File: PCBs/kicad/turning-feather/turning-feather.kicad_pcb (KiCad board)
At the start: 2 copper layers, 64.8 x 52.6 mm, 21 parts, among them J1 Out to RJ45, J2 Buttons/beep, J3 Off switch, U1 TSR 1-2450, U2 MIC4427, U3 MIC4427, U4 ZPT

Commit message: Add serial output from ZPT to serial in on feather. PCB V0.23.
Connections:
- U4 pad 6: Net-(U4-Pad6) -> Net-(JP1-Pad14)
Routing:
- net Net-(JP1-Pad14): track 0.00 -> 12.3 mm
- net +12V: track 43.0 -> 51.2 mm
- net Net-(D1-Pad2): track 4.27 -> 8.55 mm
- net Net-(JP1-Pad23): track 40.9 -> 44.3 mm
- net Net-(J2-Pad3): track 41.3 -> 43.0 mm
- net (no net): track 0.76 -> 0.00 mm
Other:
- board text added: "V0.23"
- board text removed: "V0.21"

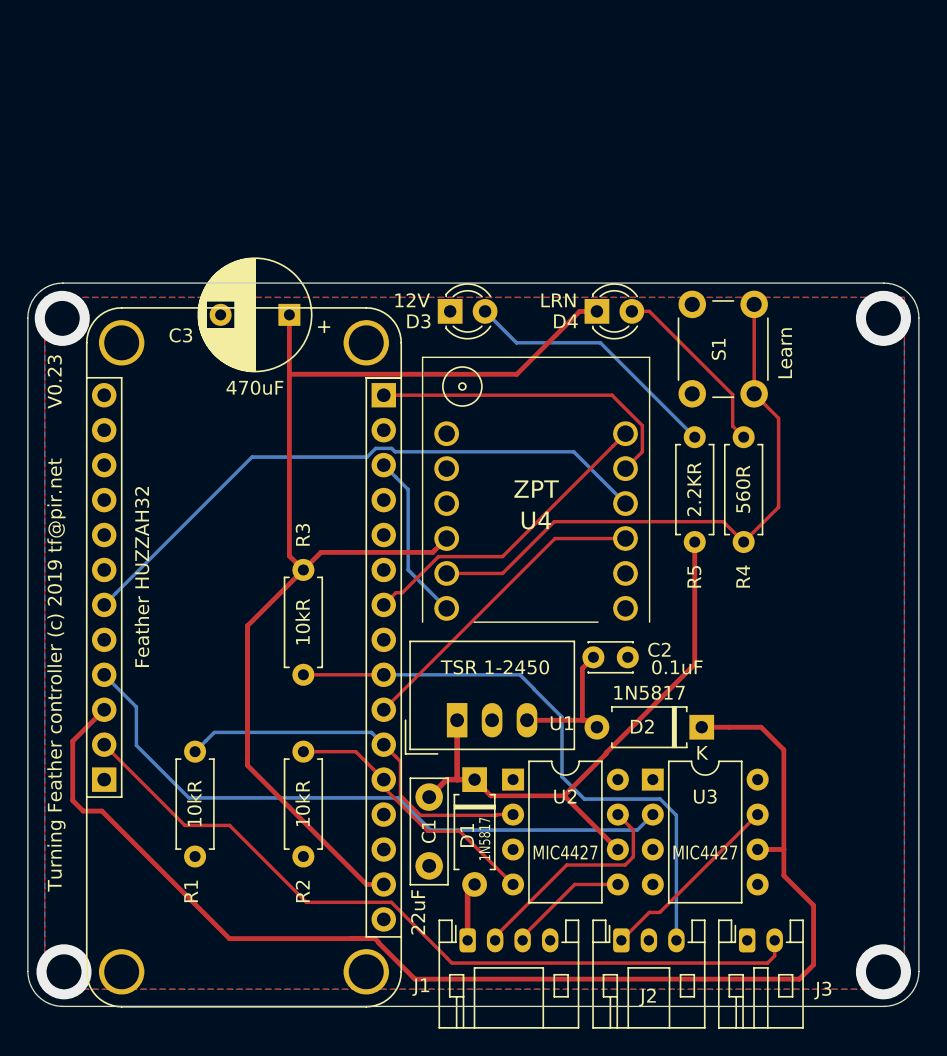
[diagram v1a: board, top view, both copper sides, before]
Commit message: PCB version 0.32.
Add serial connection from ZPT to Serial2 on HUZZAH32.
Connect spare 5V MOSFET input to spare HUZZAH32 output with header.
Add on-board PCB mount RJ45 as an option, old connector retained.
Move LEDs out to new board extension back to point towards user.
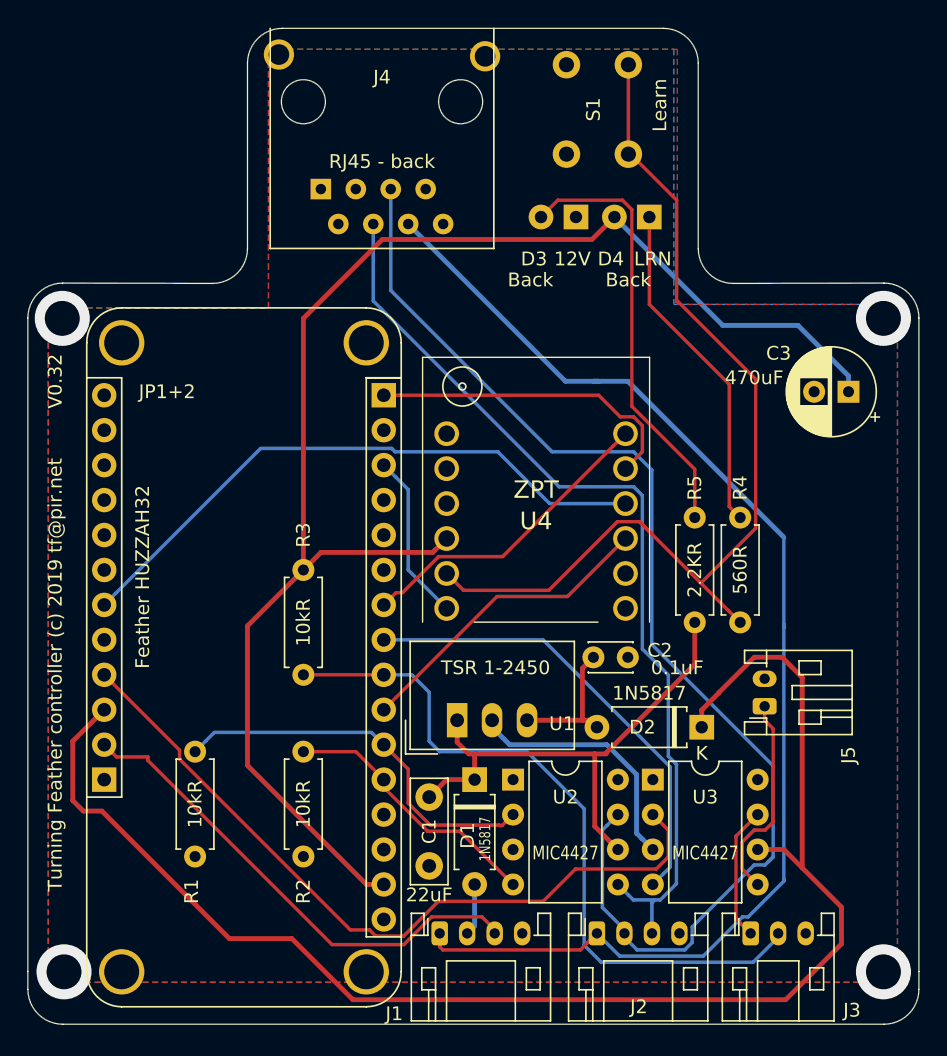
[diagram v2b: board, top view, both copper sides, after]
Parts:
- removed the J2 at (147.8, 160.8)
- added J1: Out to power switch, Connector_JST:JST_PH_S4B-PH-K_1x04_P2.00mm_Horizontal, F.Cu at (134.6, 160.3)
- added J4: RJ45_Shielded, turning-feather:RJ45_Horizontal_Shielded, B.Cu at (126.0, 106.2)
- added J5: Currently unused, Connector_JST:JST_PH_S2B-PH-K_1x02_P2.00mm_Horizontal, F.Cu at (158.2, 143.8)
- C3: footprint Capacitor_THT:CP_Radial_D8.0mm_P5.00mm -> Capacitor_THT:CP_Radial_D6.3mm_P2.50mm
- D3, D4, S1: moved to B.Cu
- J3: value Off switch -> Buttons/beep; footprint Connector_JST:JST_PH_S2B-PH-K_1x02_P2.00mm_Horizontal -> Connector_JST:JST_PH_S3B-PH-K_1x03_P2.00mm_Horizontal
- moved C3 41.0 mm to (164.3, 120.9)
- moved S1 14.2 mm to (148.3, 103.6), turned to 90 degrees
- moved D3 11.4 mm to (144.5, 108.2), turned to 180 degrees
- moved J2 9.41 mm to (146.1, 160.3)
- moved D4 7.85 mm to (149.9, 108.2), turned to 180 degrees
- moved R4 5.85 mm to (156.5, 137.7)
- moved R5 5.84 mm to (153.2, 137.7)
- moved J3 0.57 mm to (157.2, 160.3)
- renumbered J1 to J2, JP1 to JP1+2
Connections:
- D4 pad 1: +3V3 -> Net-(D4-Pad1)
- D4 pad 2: Net-(D4-Pad2) -> +3V3
- J2 pad 1: Net-(D1-Pad2) -> Net-(J1-Pad1)
- J3 pad 1: GND -> Net-(J3-Pad1)
- JP1+2 pad 27: Net-(J3-Pad2) -> Net-(J1-Pad3)
- JP1+2 pad 8: Net-(J2-Pad3) (its old number) -> Net-(J3-Pad2)
- JP1+2 pad 9: Net-(JP1-Pad9) -> Net-(JP1+2-Pad9)
- R3 pad 2: Net-(J2-Pad3) (its old number) -> Net-(J3-Pad2)
- R4 pad 2: Net-(D4-Pad2) -> Net-(D4-Pad1)
- U3 pad 4: Net-(U3-Pad4) -> Net-(JP1+2-Pad9)
- U3 pad 7: Net-(J2-Pad1) -> Net-(J3-Pad1)
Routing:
- net Net-(J1-Pad1): track 0.00 -> 91.9 mm
- net Net-(J2-Pad2): track 16.3 -> 88.7 mm
- net Net-(J2-Pad3): track 8.77 -> 68.0 mm
- net Net-(J2-Pad3) (its old number): track 43.0 -> 0.00 mm
- net Net-(J1-Pad3): track 0.00 -> 36.0 mm
- net Net-(JP1+2-Pad9): track 0.00 -> 33.7 mm
- net Net-(R4-Pad1): track 42.8 -> 71.2 mm
- net Net-(D4-Pad1): track 0.00 -> 24.6 mm
- net +3V3: track 84.0 -> 107.6 mm
- net GND: track 0.00 -> 18.9 mm
- net Net-(J5-Pad1): track 0.00 -> 15.1 mm
- net Net-(J2-Pad1): track 13.7 -> 0.00 mm
- net Net-(D4-Pad2): track 13.3 -> 0.00 mm
- net +12V: track 51.2 -> 38.4 mm
- net Net-(D3-Pad2): track 19.0 -> 31.7 mm
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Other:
- board size 64.8 x 52.6 mm -> 64.8 x 72.4 mm
- board text added: "12V in"
- board text added: "12V out"
- board text added: "Back"
- board text added: "V0.32"
- board text removed: "V0.23"

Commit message: Move ethernet on-PCB, move most things around, change capacitors, etc
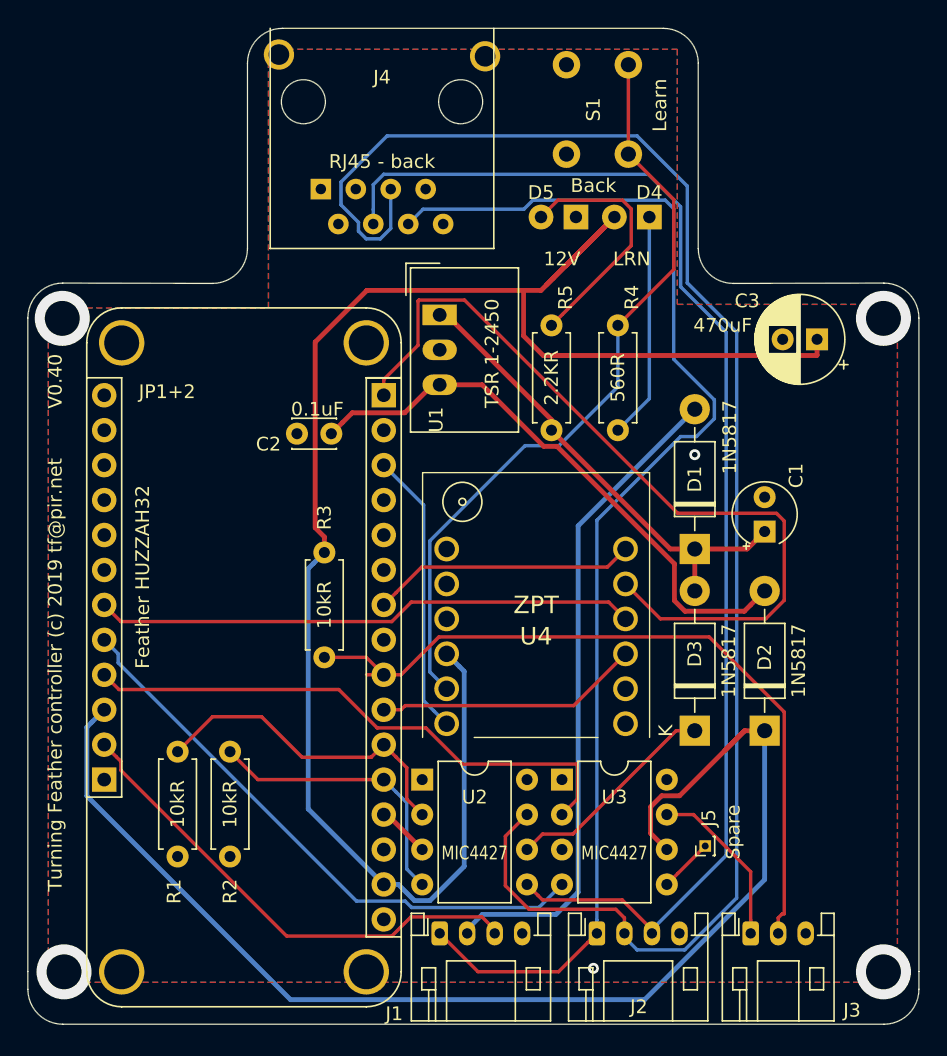
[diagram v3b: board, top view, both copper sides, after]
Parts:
- added D3: 1N5817, Diode_THT:D_DO-41_SOD81_P10.16mm_Horizontal, F.Cu at (153.2, 145.5)
- C1: footprint Capacitor_THT:C_Disc_D7.5mm_W2.5mm_P5.00mm -> Capacitor_THT:CP_Radial_Tantal_D4.5mm_P2.50mm
- D1, D2: footprint Diode_THT:D_A-405_P7.62mm_Horizontal -> Diode_THT:D_DO-41_SOD81_P10.16mm_Horizontal
- J5: value Currently unused -> Spare; footprint Connector_JST:JST_PH_S2B-PH-K_1x02_P2.00mm_Horizontal -> Connector_PinHeader_1.00mm:PinHeader_1x01_P1.00mm_Vertical
- moved C1 31.1 mm to (158.2, 131.1), turned to 90 degrees
- moved U1 29.5 mm to (134.6, 115.3), turned to 270 degrees
- moved C2 25.0 mm to (126.7, 124.0), turned to 180 degrees
- moved R5 24.0 mm to (142.7, 116.1), turned to 270 degrees
- moved R4 23.3 mm to (147.6, 116.1), turned to 270 degrees
- moved D1 23.2 mm to (153.2, 132.3), turned to 90 degrees
- moved J5 11.0 mm to (153.9, 153.9)
- moved U4 8.38 mm to (135.1, 132.3)
- moved U2 6.60 mm to (133.3, 149.1)
- moved U3 6.60 mm to (143.5, 149.1)
- moved R2 5.33 mm to (119.4, 147.1)
- moved D2 4.58 mm to (158.2, 145.5), turned to 90 degrees
- moved C3 4.44 mm to (162.1, 117.1)
- moved R3 1.98 mm to (126.2, 132.6)
- moved R1 1.27 mm to (115.6, 147.1)
- renumbered D3 to D5
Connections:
- D5 pad 2: Net-(D3-Pad2) -> Net-(D5-Pad2)
- R5 pad 1: +12V -> Net-(D5-Pad2)
- R5 pad 2: Net-(D3-Pad2) -> +12V
- U2 pad 6: +12V -> Net-(D3-Pad1)
- U3 pad 4: Net-(JP1+2-Pad9) -> Net-(JP1+2-Pad24)
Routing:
- net Net-(D1-Pad2): track 3.78 -> 48.7 mm
- net Net-(JP1+2-Pad24): track 0.00 -> 42.4 mm
- net Net-(JP1+2-Pad16): track 23.3 -> 60.1 mm
- net Net-(JP1+2-Pad9): track 33.7 -> 0.00 mm
- net Net-(C2-Pad1): track 10.2 -> 42.0 mm
- net Net-(D3-Pad2): track 31.7 -> 0.00 mm
- net Net-(J2-Pad2): track 88.7 -> 118.1 mm
- net Net-(J2-Pad3): track 68.0 -> 93.6 mm
- net +3V3: track 107.6 -> 130.7 mm
- net Net-(D5-Pad2): track 0.00 -> 18.2 mm
- net Net-(D3-Pad1): track 0.00 -> 15.8 mm
- net Net-(R4-Pad1): track 71.2 -> 56.0 mm
- net GND: track 18.9 -> 4.40 mm, vias 4 -> 6
- net Net-(JP1+2-Pad25): track 55.2 -> 41.2 mm
- net +5V: track 106.2 -> 92.9 mm
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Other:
- board text added: "V0.40"
- board text removed: "V0.32"
